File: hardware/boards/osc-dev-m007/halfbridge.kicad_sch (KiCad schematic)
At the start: 11 parts, among them Q401 SIL3724A-TP

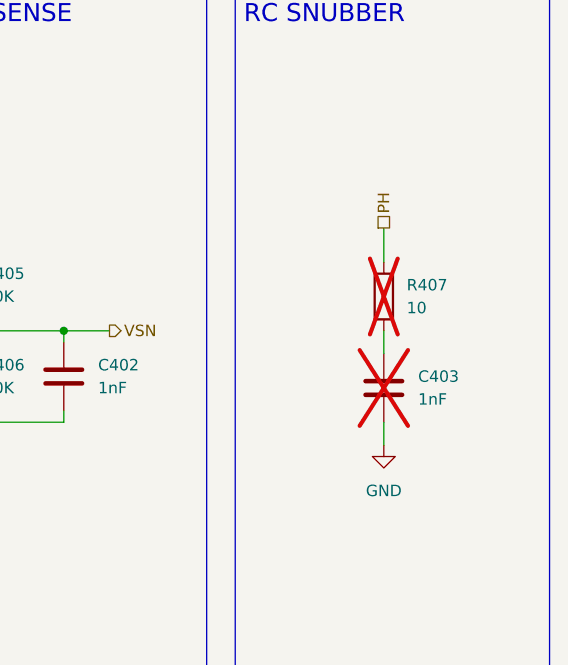
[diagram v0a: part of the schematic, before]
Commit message: hw: design osc-dev-m007 pcb
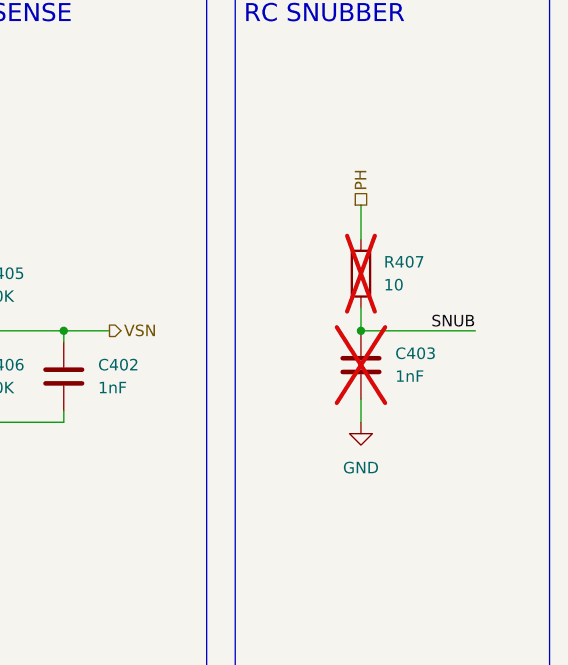
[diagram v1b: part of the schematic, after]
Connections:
- net SNUB: now reaches C403.1, R407.2
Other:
- moved on the sheet: C403, R407
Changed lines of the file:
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@@
+	)
+	(junction
+		(at 143.51 66.04)
+		(diameter 0)
+		(color 0 0 0 0)
 	)
 	(junction
@@
 	(wire
 		(pts
-			(xy 146.05 76.2) (xy 146.05 78.74)
+			(xy 143.51 73.66) (xy 143.51 76.2)
 		)
 		(stroke
@@
 	(wire
 		(pts
+			(xy 143.51 63.5) (xy 143.51 66.04)
+		)
+		(stroke
+			(width 0)
+			(type default)
+		)
+	)
+	(wire
+		(pts
 			(xy 35.56 72.39) (xy 38.1 72.39)
 		)
@@
 	(wire
 		(pts
+			(xy 156.21 66.04) (xy 143.51 66.04)
+		)
+		(stroke
+			(width 0)
+			(type default)
+		)
+	)
+	(wire
+		(pts
 			(xy 99.06 77.47) (xy 99.06 76.2)
 		)
@@
 	(wire
 		(pts
-			(xy 146.05 58.42) (xy 146.05 54.61)
+			(xy 143.51 55.88) (xy 143.51 52.07)
 		)
 		(stroke
@@
 		(pts
 			(xy 54.61 49.53) (xy 54.61 54.61)
-		)
-		(stroke
-			(width 0)
-			(type default)
-		)
-	)
-	(wire
-		(pts
-			(xy 146.05 66.04) (xy 146.05 68.58)
 		)
 		(stroke
@@
 		)
 	)
+	(label "SNUB"
+		(at 156.21 66.04 180)
+		(effects
+			(font
+				(size 1.27 1.27)
+			)
+			(justify right bottom)
+		)
+	)
 	(label "G_H"
 		(at 43.18 59.69 0)
@@
 	(hierarchical_label "PH"
 		(shape passive)
-		(at 146.05 54.61 90)
+		(at 143.51 52.07 90)
 		(effects
 			(font
@@
 	(symbol
 		(lib_id "Device:C")
-		(at 146.05 72.39 0)
+		(at 143.51 69.85 0)
 		(unit 1)
 		(body_style 1)
@@
 		(fields_autoplaced yes)
 		(property "Reference" "C403"
-			(at 149.86 71.1199 0)
+			(at 147.32 68.5799 0)
 			(show_name no)
 			(do_not_autoplace no)
@@
 		)
 		(property "Value" "1nF"
-			(at 149.86 73.6599 0)
+			(at 147.32 71.1199 0)
 			(show_name no)
 			(do_not_autoplace no)
@@
 		)
 		(property "Footprint" "Capacitor_SMD:C_0805_2012Metric_Pad1.18x1.45mm_HandSolder"
-			(at 147.0152 76.2 0)
+			(at 144.4752 73.66 0)
 			(hide yes)
 			(show_name no)
@@
 		)
 		(property "Datasheet" "https://www.lcsc.com/product-detail/C46653.html"
-			(at 146.05 72.39 0)
+			(at 143.51 69.85 0)
 			(hide yes)
 			(show_name no)
@@
 		)
 		(property "Description" "Unpolarized capacitor"
-			(at 146.05 72.39 0)
+			(at 143.51 69.85 0)
 			(hide yes)
 			(show_name no)
@@
 		)
 		(property "MFPN" "CL21B102KBCNNNC"
-			(at 146.05 72.39 0)
+			(at 143.51 69.85 0)
 			(hide yes)
 			(show_name no)
@@
 		)
 		(property "JLC_Basic" "yes"
-			(at 146.05 72.39 0)
+			(at 143.51 69.85 0)
 			(hide yes)
 			(show_name no)
@@
 		)
 		(property "LCSC" "C46653"
-			(at 146.05 72.39 0)
+			(at 143.51 69.85 0)
 			(hide yes)
 			(show_name no)
@@
 	(symbol
 		(lib_id "power:GND")
-		(at 146.05 78.74 0)
+		(at 143.51 76.2 0)
 		(unit 1)
 		(body_style 1)
@@
 		(fields_autoplaced yes)
 		(property "Reference" "#PWR0404"
-			(at 146.05 85.09 0)
+			(at 143.51 82.55 0)
 			(hide yes)
 			(show_name no)
@@
 		)
 		(property "Value" "GND"
-			(at 146.05 83.82 0)
+			(at 143.51 81.28 0)
 			(show_name no)
 			(do_not_autoplace no)
@@
 		)
 		(property "Footprint" ""
-			(at 146.05 78.74 0)
+			(at 143.51 76.2 0)
 			(hide yes)
 			(show_name no)
@@
 		)
 		(property "Datasheet" ""
-			(at 146.05 78.74 0)
+			(at 143.51 76.2 0)
 			(hide yes)
 			(show_name no)
@@
 		)
 		(property "Description" "Power symbol creates a global label with name \"GND\" , ground"
-			(at 146.05 78.74 0)
+			(at 143.51 76.2 0)
 			(hide yes)
 			(show_name no)
@@
 	(symbol
 		(lib_id "Device:R")
-		(at 146.05 62.23 0)
+		(at 143.51 59.69 0)
 		(unit 1)
 		(body_style 1)
@@
 		(fields_autoplaced yes)
 		(property "Reference" "R407"
-			(at 148.59 60.9599 0)
+			(at 146.05 58.4199 0)
 			(show_name no)
 			(do_not_autoplace no)
@@
 		)
 		(property "Value" "10"
-			(at 148.59 63.4999 0)
+			(at 146.05 60.9599 0)
 			(show_name no)
 			(do_not_autoplace no)
@@
 		)
 		(property "Footprint" "Resistor_SMD:R_0805_2012Metric_Pad1.20x1.40mm_HandSolder"
-			(at 144.272 62.23 90)
+			(at 141.732 59.69 90)
 			(hide yes)
 			(show_name no)
@@
 		)
 		(property "Datasheet" "https://www.lcsc.com/product-detail/C17415.html"
-			(at 146.05 62.23 0)
+			(at 143.51 59.69 0)
 			(hide yes)
 			(show_name no)
@@
 		)
 		(property "Description" "Resistor"
-			(at 146.05 62.23 0)
+			(at 143.51 59.69 0)
 			(hide yes)
 			(show_name no)
@@
 		)
 		(property "MFPN" "0805W8F100JT5E"
-			(at 146.05 62.23 0)
+			(at 143.51 59.69 0)
 			(hide yes)
 			(show_name no)
@@
 		)
 		(property "JLC_Basic" "yes"
-			(at 146.05 62.23 0)
+			(at 143.51 59.69 0)
 			(hide yes)
 			(show_name no)
@@
 		)
 		(property "LCSC" "C17415"
-			(at 146.05 62.23 0)
-			(hide yes)
-			(show_name no)
+			(at 143.51 59.69 0)
+			(hide yes)
+			(show_name no)

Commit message: hw: add osc-sg90-m007 renders to readme
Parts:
- R403, R404: value 100K -> 100k
- R405: value 20K -> 20k
- R406: value 10K -> 10k
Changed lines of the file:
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@@
 			)
 		)
-		(property "Value" "10K"
+		(property "Value" "10k"
 			(at 101.6 72.3899 0)
 			(show_name no)
@@
 			)
 		)
-		(property "Value" "20K"
+		(property "Value" "20k"
 			(at 101.6 62.2299 0)
 			(show_name no)
@@
 			)
 		)
-		(property "Value" "100K"
+		(property "Value" "100k"
 			(at 39.37 78.486 0)
 			(show_name no)
@@
 			)
 		)
-		(property "Value" "100K"
+		(property "Value" "100k"
 			(at 39.624 55.626 0)
 			(show_name no)

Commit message: hw: swap dev-m007 parts to in-stock equivalents
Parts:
- C402, C403: LCSC C46653 -> C94121; MFPN CL21B102KBCNNNC -> CC0805KRX7R9BB102
- R406: LCSC C17414 -> C2907219; MFPN 0805W8F1002T5E -> FRC0805F1002TS
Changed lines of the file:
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@@
 			)
 		)
-		(property "Datasheet" "https://www.lcsc.com/product-detail/C46653.html"
+		(property "Datasheet" "https://www.lcsc.com/product-detail/C94121.html"
 			(at 143.51 69.85 0)
 			(hide yes)
@@
 			)
 		)
-		(property "MFPN" "CL21B102KBCNNNC"
+		(property "MFPN" "CC0805KRX7R9BB102"
 			(at 143.51 69.85 0)
 			(hide yes)
@@
 			)
 		)
-		(property "LCSC" "C46653"
+		(property "LCSC" "C94121"
 			(at 143.51 69.85 0)
 			(hide yes)
@@
 			)
 		)
-		(property "Datasheet" "https://www.lcsc.com/product-detail/C17414.html"
+		(property "Datasheet" "https://www.lcsc.com/product-detail/C2907219.html"
 			(at 99.06 71.12 0)
 			(hide yes)
@@
 			)
 		)
-		(property "MFPN" "0805W8F1002T5E"
+		(property "MFPN" "FRC0805F1002TS"
 			(at 99.06 71.12 0)
 			(hide yes)
@@
 			)
 		)
-		(property "LCSC" "C17414"
+		(property "LCSC" "C2907219"
 			(at 99.06 71.12 0)
 			(hide yes)
@@
 			)
 		)
-		(property "Datasheet" "https://www.lcsc.com/product-detail/C46653.html"
+		(property "Datasheet" "https://www.lcsc.com/product-detail/C94121.html"
 			(at 110.49 71.12 0)
 			(hide yes)
@@
 			)
 		)
-		(property "MFPN" "CL21B102KBCNNNC"
+		(property "MFPN" "CC0805KRX7R9BB102"
 			(at 110.49 71.12 0)
 			(hide yes)
@@
 			)
 		)
-		(property "LCSC" "C46653"
+		(property "LCSC" "C94121"
 			(at 110.49 71.12 0)
 			(hide yes)
